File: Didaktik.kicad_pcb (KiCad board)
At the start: 2 copper layers, 212.7 x 79.4 mm, 104 parts, among them J1 Conn_01x04_MountingPin, SW1 SW_Push, SW10 SW_Push_45deg, SW11 SW_Push_45deg, SW12 SW_Push_45deg, SW13 SW_Push_45deg, SW14 SW_Push_45deg, SW15 SW_Push_45deg, SW16 SW_Push_45deg, SW17 SW_Push_45deg, SW18 SW_Push_45deg, SW19 SW_Push_45deg, SW2 SW_Push_45deg, SW20 SW_Push_45deg, SW21 SW_Push_45deg, SW22 SW_Push_45deg, SW23 SW_Push_45deg, SW24 SW_Push_45deg, SW25 SW_Push_45deg, SW26 SW_Push_45deg, SW27 SW_Push_45deg, SW28 SW_Push_45deg, SW29 SW_Push_45deg, SW3 SW_Push_45deg, SW30 SW_Push_45deg, SW31 SW_Push_45deg, SW32 SW_Push_45deg, SW33 SW_Push_45deg, SW34 SW_Push_45deg, SW35 SW_Push_45deg, SW36 SW_Push_45deg, SW37 SW_Push_45deg, SW38 SW_Push_45deg, SW39 SW_Push_45deg, SW4 SW_Push_45deg, SW40 SW_Push_45deg, SW41 SW_Push_45deg, SW5 SW_Push_45deg, SW6 SW_Push_45deg, SW7 SW_Push_45deg, SW8 SW_Push_45deg, SW9 SW_Push_45deg, U1 ATmega32U4-M, Y1 Crystal_GND24_Small

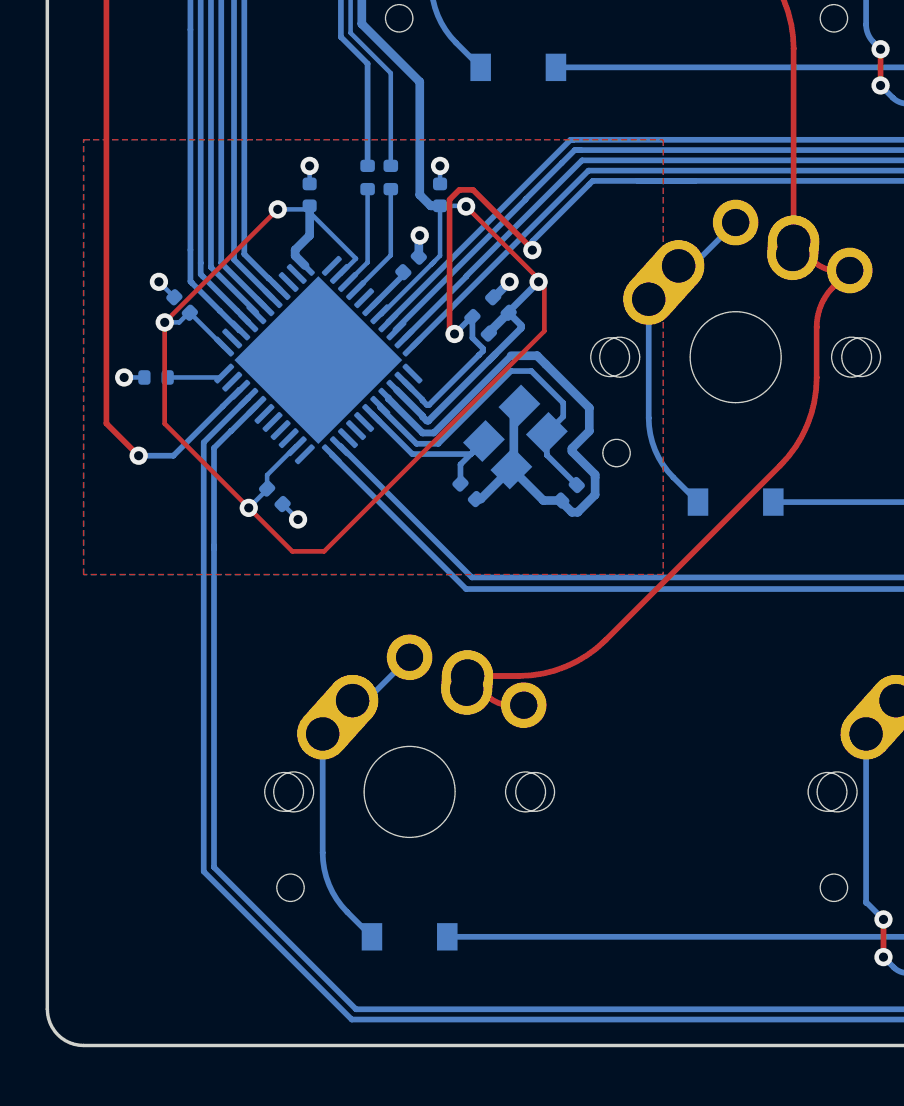
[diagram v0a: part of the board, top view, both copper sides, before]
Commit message: added ISP to 40, added ISP schematics to 45
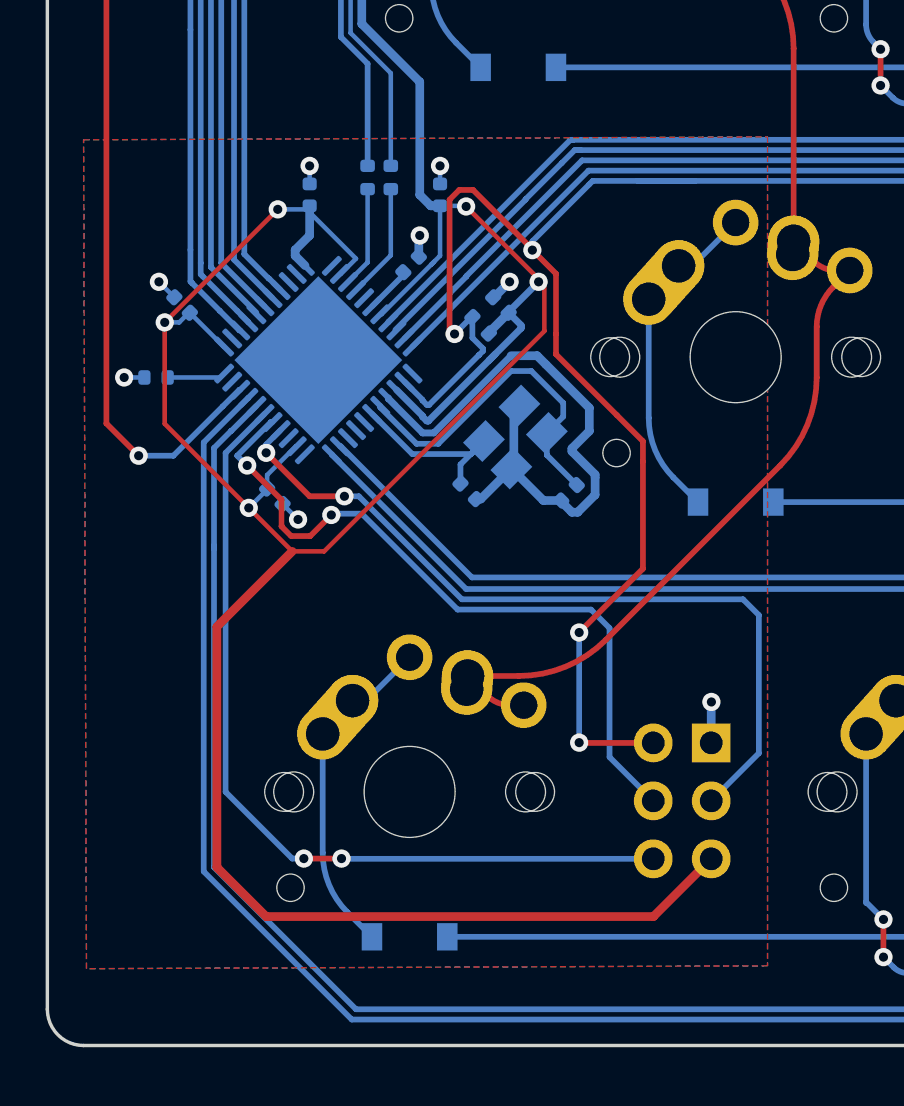
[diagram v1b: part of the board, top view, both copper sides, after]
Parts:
- added J2: AVR-ISP-6, random-keyboard-parts:Reset_Pretty-Mask, B.Cu at (58.0, 98.8)
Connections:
- net Net-(R3-Pad2) renamed RESET
- U1 pad 26: unconnected-(U1-Pad26) -> MOSI
- U1 pad 27: unconnected-(U1-Pad27) -> SCK
- U1 pad 28: unconnected-(U1-Pad28) -> MISO
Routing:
- net +5V: track 284.8 -> 323.7 mm
- net MISO: track 0.00 -> 37.2 mm, vias 0 -> 2
- net MOSI: track 0.00 -> 34.8 mm, vias 0 -> 2
- net SCK: track 0.00 -> 31.5 mm, vias 0 -> 2
- net RESET: track 221.2 -> 249.2 mm, vias 3 -> 5
- net GND: track 48.7 -> 50.4 mm, vias 13 -> 14

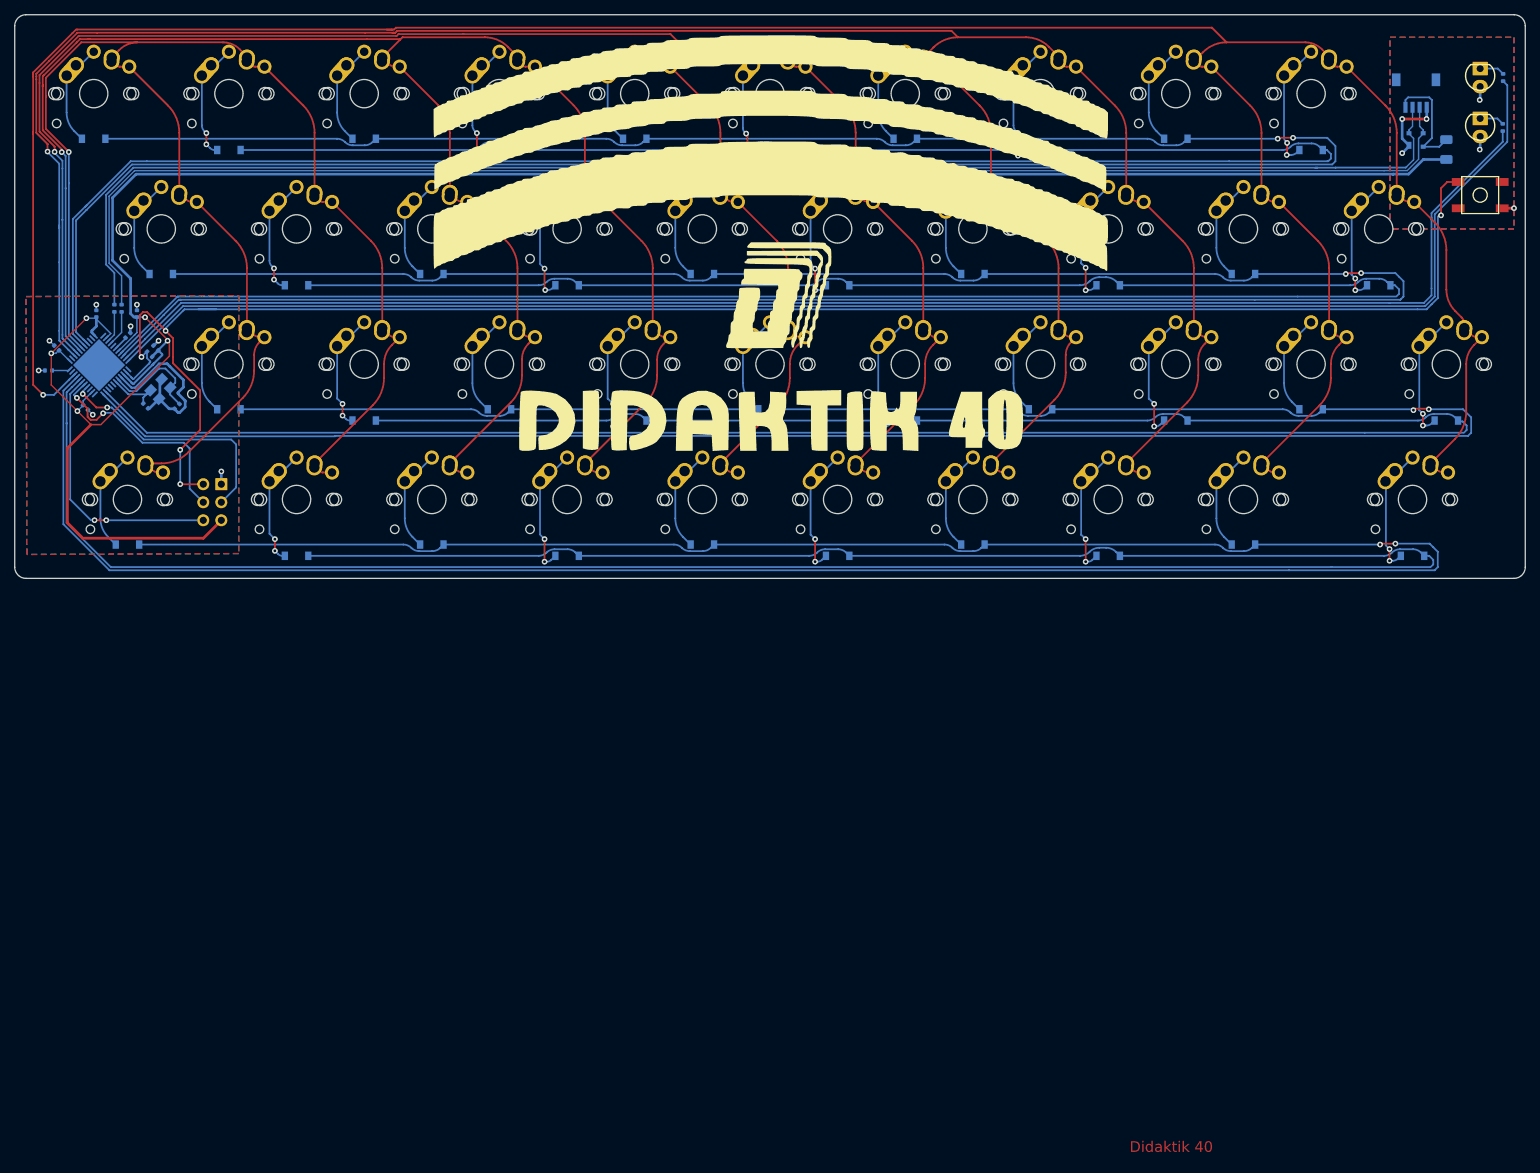
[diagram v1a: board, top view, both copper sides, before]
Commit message: cleaned up some traces, ran DRC
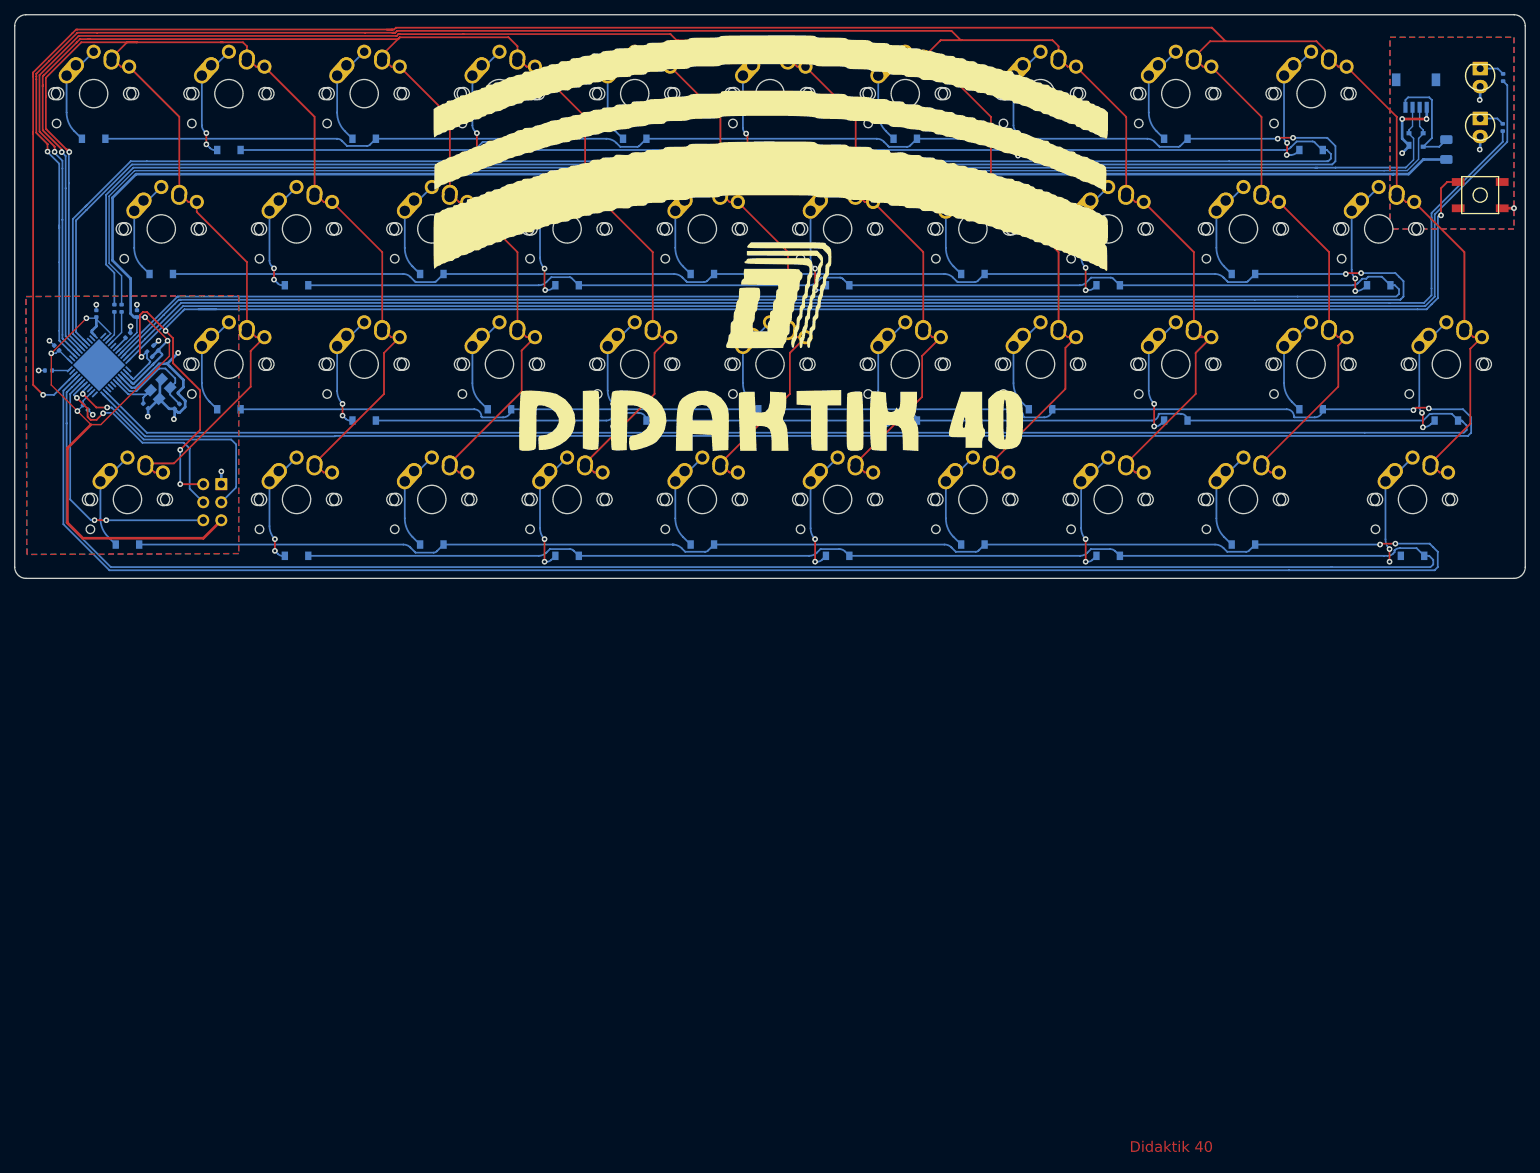
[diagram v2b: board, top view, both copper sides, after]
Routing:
- net COL3: track 346.0 -> 354.0 mm
- net GND: track 50.4 -> 55.3 mm, vias 14 -> 17
- net COL4: track 390.7 -> 395.4 mm
- net COL1: track 263.6 -> 268.2 mm
- net COL0: track 229.6 -> 234.1 mm
- net COL2: track 304.1 -> 307.6 mm
- net ROW4: track 373.6 -> 376.4 mm
- net ROW5: track 350.6 -> 352.6 mm
- net Net-(D41-Pad2): track 18.3 -> 16.7 mm
- net ROW2: track 362.0 -> 363.3 mm
- net ROW3: track 340.1 -> 341.3 mm
- net ROW0: track 376.9 -> 378.0 mm
- net ROW6: track 405.7 -> 406.8 mm
- net ROW1: track 356.6 -> 357.5 mm
- net ROW7: track 377.7 -> 378.5 mm
- added copper zone on B.Cu, net GND
- added copper zone on F.Cu, net GND
- removed copper zone on B.Cu, net (none)
- removed copper zone on F.Cu, net (none)

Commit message: updated routing, created footprints for bottom row
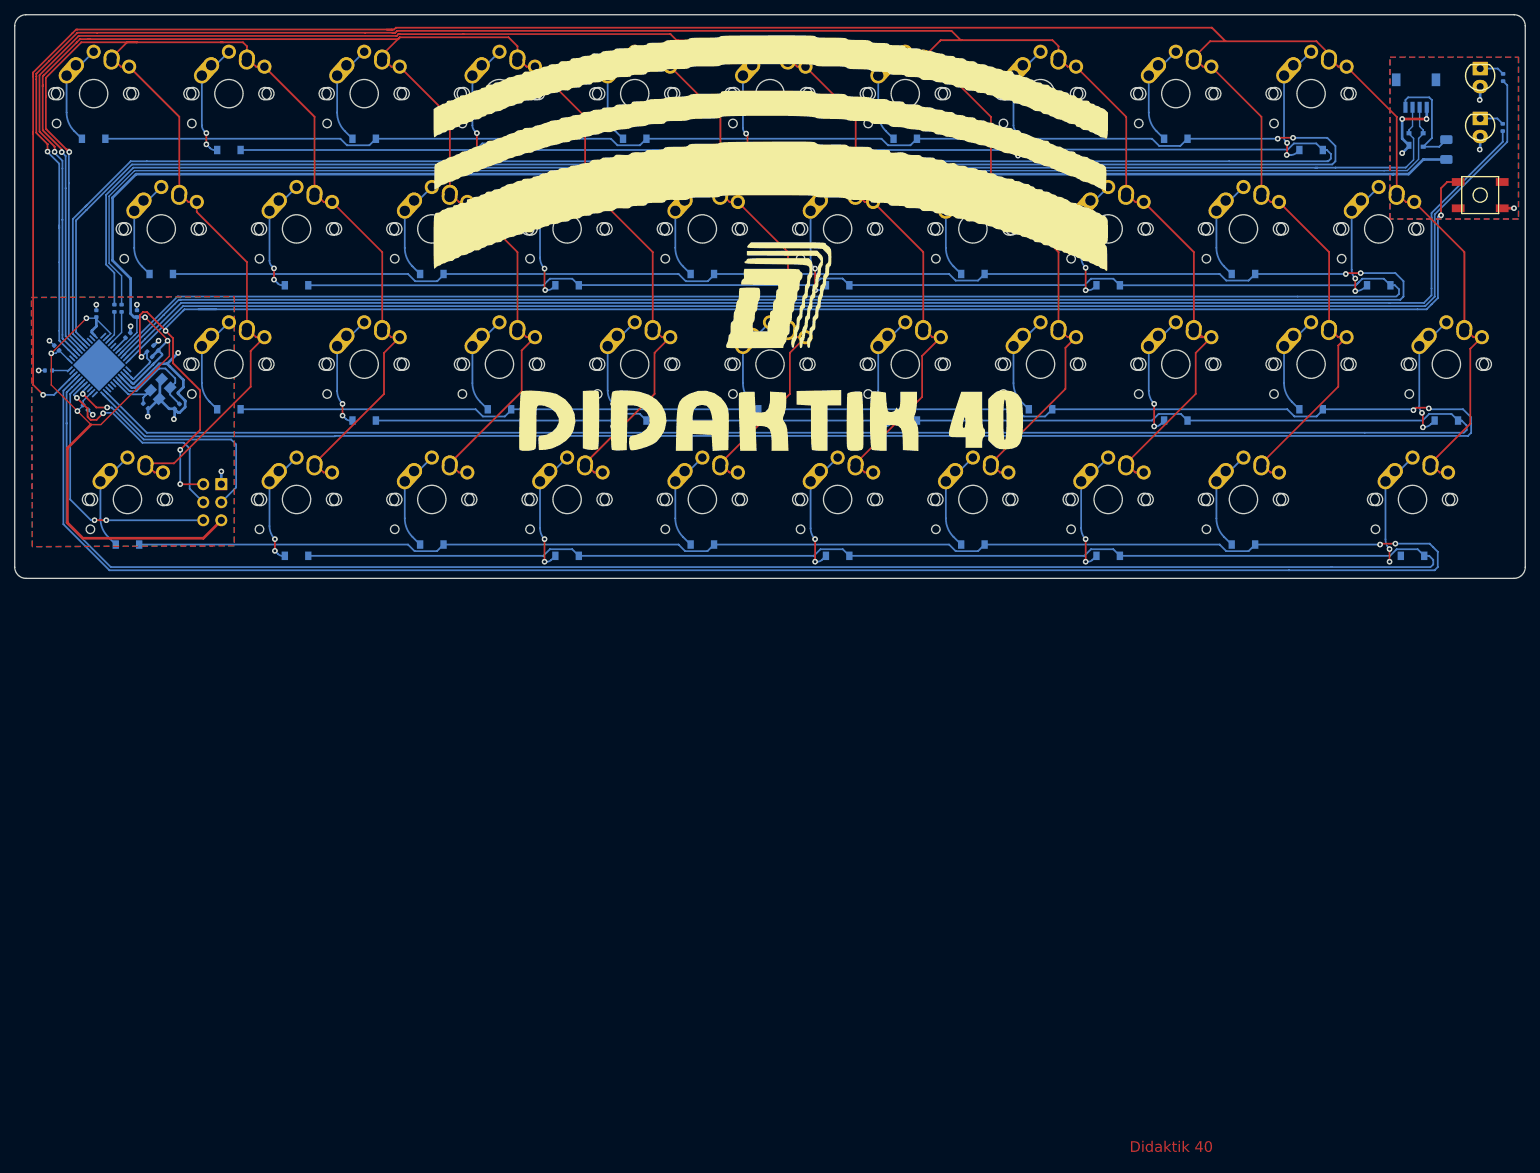
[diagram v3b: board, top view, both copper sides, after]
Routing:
- net ROW4: track 376.4 -> 374.8 mm
- net ROW5: track 352.6 -> 351.7 mm

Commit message: cleaned routing, added multilayout to schematics and laid out footprints under the pcb
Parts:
- added SW31a1: SW_Push_45deg, Keebio-Parts:MX-Alps-Choc-1U-NoLED, F.Cu at (41.3, 122.2)
- added SW32a1: SW_Push_45deg, Keebio-Parts:MX-Alps-Choc-1U-NoLED, F.Cu at (60.3, 122.2)
- added SW33a1: SW_Push_45deg, Keebio-Parts:MX-Alps-Choc-1U-NoLED, F.Cu at (79.4, 122.2)
- added SW34a1: SW_Push_45deg, Keebio-Parts:MX-Alps-Choc-1U-NoLED, F.Cu at (98.4, 122.2)
- added SW34b1: SW_Push_45deg, Keebio-Parts:MX-Alps-Choc-3U-NoLED-StabFlip, F.Cu at (108.0, 122.2)
- added SW35a1: SW_Push_45deg, Keebio-Parts:MX-Alps-Choc-1.5U-NoLED, F.Cu at (122.2, 122.2)
- added SW35b1: SW_Push_45deg, Keebio-Parts:MX-Alps-Choc-2U-NoLED-StabFlip, F.Cu at (117.5, 122.2)
- added SW35c1: SW_Push_45deg, Keebio-Parts:MX-Alps-Choc-6U-NoLED-StabFlip, F.Cu at (136.5, 122.2)
- added SW36a1: SW_Push_45deg, Keebio-Parts:MX-Alps-Choc-1.5U-NoLED, F.Cu at (150.8, 122.2)
- added SW36b1: SW_Push_45deg, Keebio-Parts:MX-Alps-Choc-2U-NoLED-StabFlip, F.Cu at (155.6, 122.2)
- added SW36c1: SW_Push_45deg, Keebio-Parts:MX-Alps-Choc-7U-NoLED-StabFlip, F.Cu at (136.5, 122.2)
- added SW37a1: SW_Push_45deg, Keebio-Parts:MX-Alps-Choc-1U-NoLED, F.Cu at (174.6, 122.2)
- added SW37b1: SW_Push_45deg, Keebio-Parts:MX-Alps-Choc-3U-NoLED-StabFlip, F.Cu at (165.1, 122.2)
- added SW38a1: SW_Push_45deg, Keebio-Parts:MX-Alps-Choc-1U-NoLED, F.Cu at (193.7, 122.2)
- added SW39a1: SW_Push_45deg, Keebio-Parts:MX-Alps-Choc-1U-NoLED, F.Cu at (212.7, 122.2)
- added SW40a1: SW_Push_45deg, Keebio-Parts:MX-Alps-Choc-1U-NoLED, F.Cu at (231.8, 122.2)
- SW31: renamed from SW5; footprint Keebio-Parts:MX-Alps-Choc-1U-NoLED -> Keebio-Parts:MX-Alps-Choc-1.5U-NoLED
- SW40: renamed from SW41; footprint Keebio-Parts:MX-Alps-Choc-1U-NoLED -> Keebio-Parts:MX-Alps-Choc-1.5U-NoLED
- renumbered SW2 to SW1, SW38 to SW10, SW3 to SW11, SW7 to SW12, SW11 to SW13, SW15 to SW14, SW19 to SW15, SW23 to SW16, SW27 to SW17, SW31 to SW18, SW35 to SW19, SW6 to SW2, SW39 to SW20, SW4 to SW21, SW8 to SW22, SW12 to SW23, SW16 to SW24, SW20 to SW25, SW24 to SW26, SW28 to SW27, SW32 to SW28, SW36 to SW29, SW10 to SW3, SW40 to SW30, SW9 to SW32, SW13 to SW33, SW17 to SW34, SW21 to SW35, SW25 to SW36, SW29 to SW37, SW33 to SW38, SW37 to SW39, SW14 to SW4, SW18 to SW5, SW22 to SW6, SW26 to SW7, SW30 to SW8, SW34 to SW9, SW1 to SW_Reset1
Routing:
- net Net-(D41-Pad2): track 16.7 -> 18.5 mm
- net Net-(D7-Pad2): track 16.8 -> 18.5 mm
- net Net-(D8-Pad2): track 16.8 -> 18.5 mm
- net Net-(D6-Pad2): track 16.8 -> 18.4 mm
- net Net-(D5-Pad2): track 16.8 -> 18.3 mm
- net ROW4: track 374.8 -> 374.4 mm, vias 2 -> 0
- net ROW0: track 377.8 -> 377.7 mm, vias 2 -> 0
- net ROW6: track 406.6 -> 406.5 mm, vias 2 -> 0
- net ROW2: track 363.1 -> 363.0 mm, vias 2 -> 0

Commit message: changes
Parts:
- removed SW31a1, SW32a1, SW33a1, SW34a1, SW37a1, SW38a1, SW39a1, SW40a1: SW_Push_45deg, Keebio-Parts:MX-Alps-Choc-1U-NoLED
- removed SW34b1, SW37b1: SW_Push_45deg, Keebio-Parts:MX-Alps-Choc-3U-NoLED-StabFlip
- removed SW35a1, SW36a1: SW_Push_45deg, Keebio-Parts:MX-Alps-Choc-1.5U-NoLED
- removed SW35b1, SW36b1: SW_Push_45deg, Keebio-Parts:MX-Alps-Choc-2U-NoLED-StabFlip
- removed SW35c1: SW_Push_45deg, Keebio-Parts:MX-Alps-Choc-6U-NoLED-StabFlip
- removed SW36c1: SW_Push_45deg, Keebio-Parts:MX-Alps-Choc-7U-NoLED-StabFlip
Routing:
- net (no net): track 0.00 -> 8.97 mm, vias 0 -> 2
